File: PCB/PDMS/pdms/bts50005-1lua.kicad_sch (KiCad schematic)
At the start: 11 parts, among them Q3 BTS500101LUAAUMA1

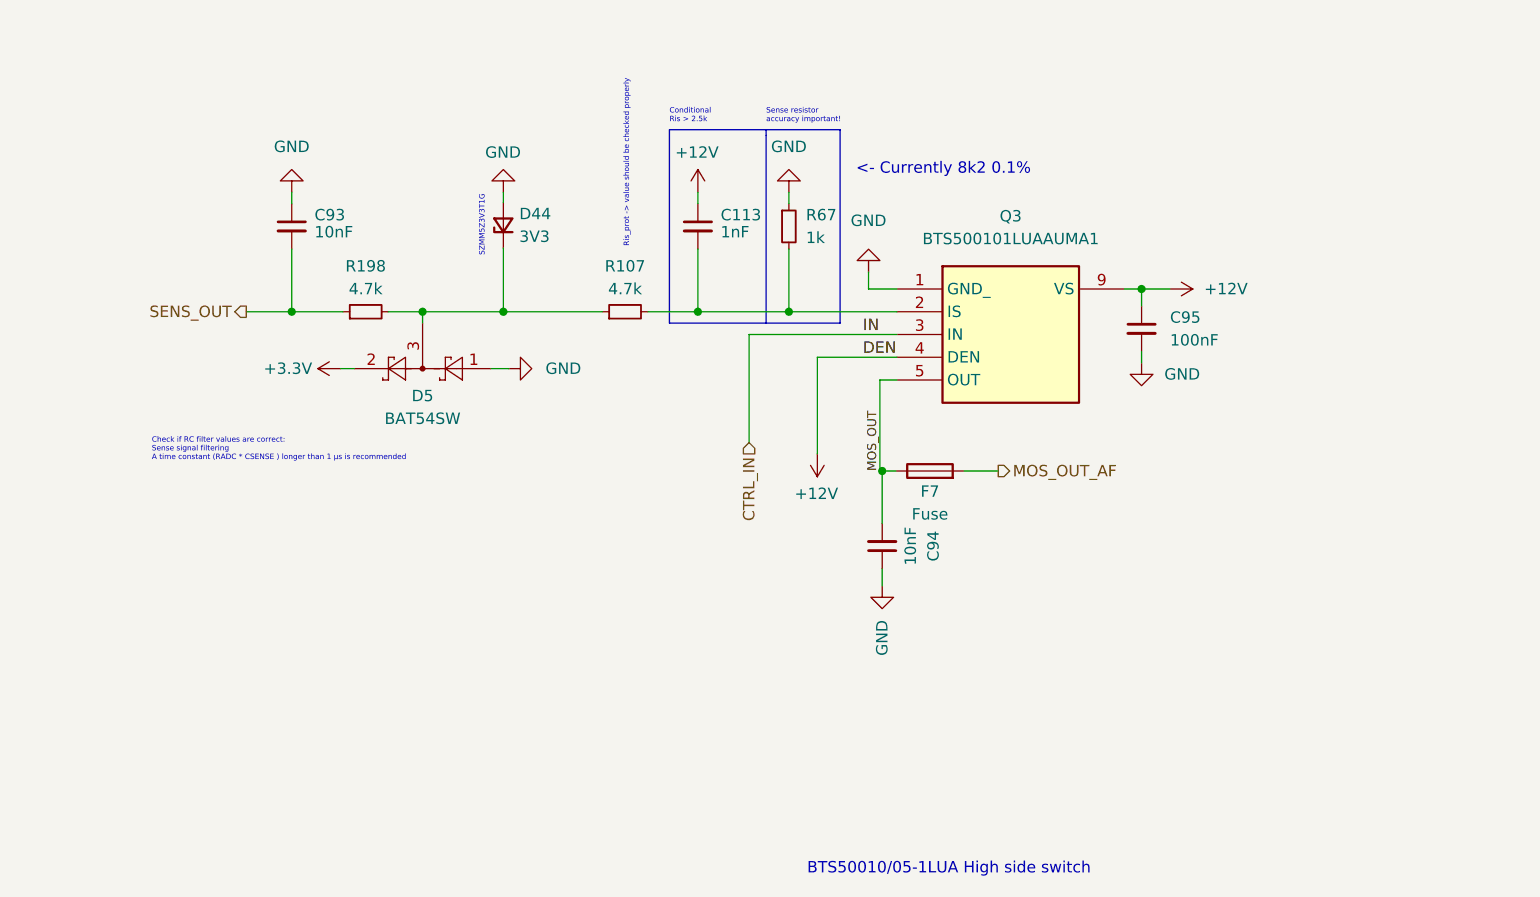
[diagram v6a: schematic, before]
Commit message: WIP PCB folder structure and schematic clean-up
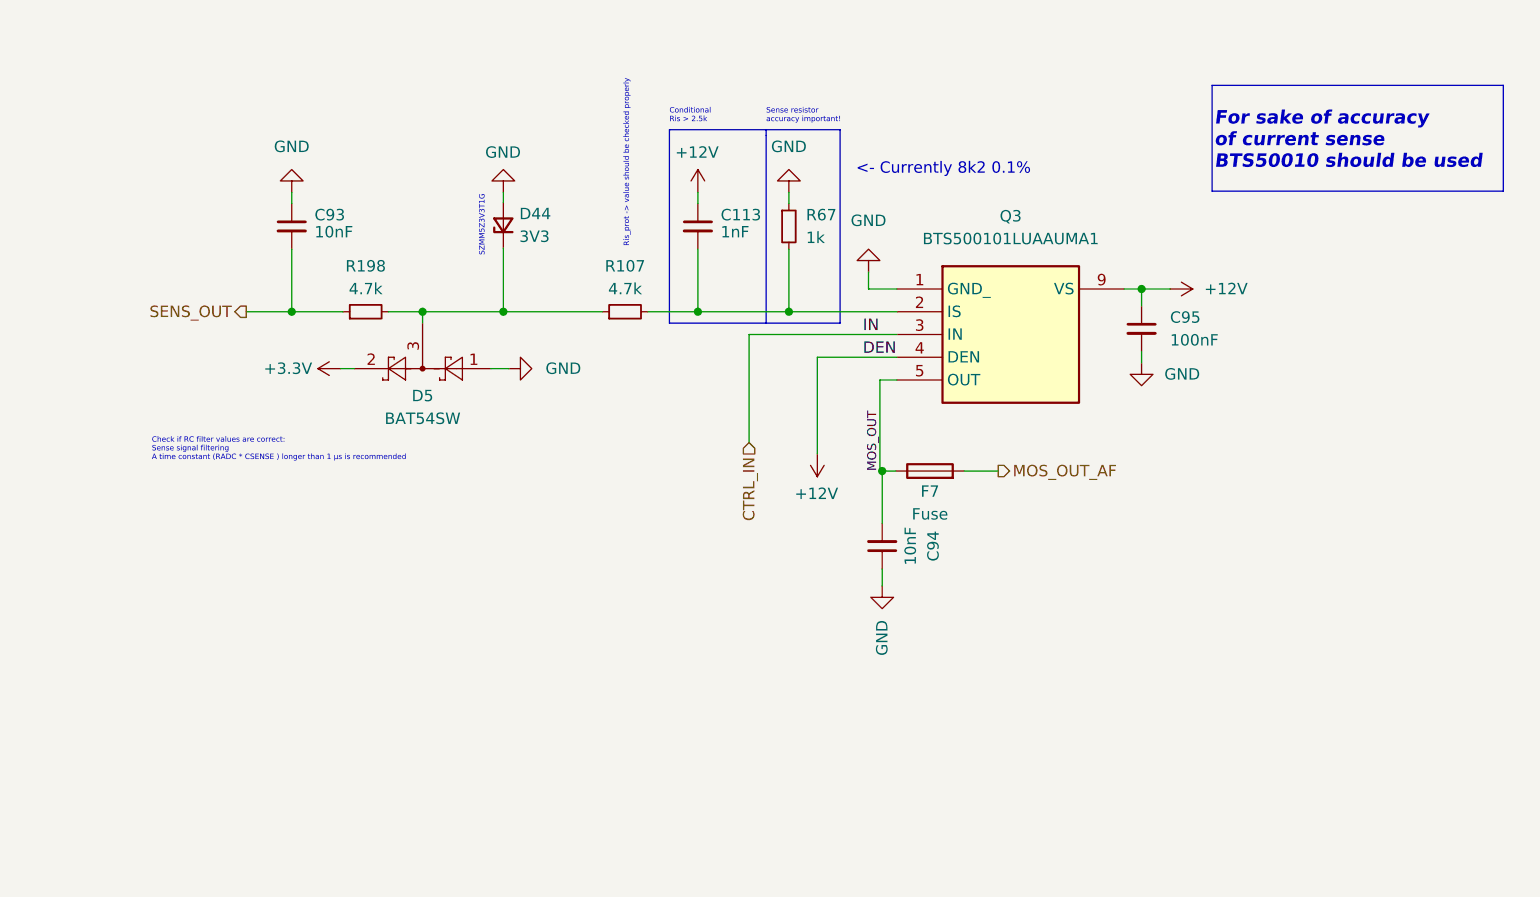
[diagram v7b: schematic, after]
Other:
- note added: "For sake of accuracy of current sense BTS50010 should be used"
- note removed: "BTS50010/05-1LUA High side switch"
- company: (none) -> PGRacing Team
- title: (none) -> BTS50010/05-1LUA High side switch 
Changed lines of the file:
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@@
 (kicad_sch (version 20211123) (generator eeschema)
   (paper "A5")
+  (title_block
+    (title "BTS50010/05-1LUA High side switch ")
+    (rev "V4.2")
+    (company "PGRacing Team")
+    (comment 1 "Karol Pergoł")
+  )
   (junction (at 137.668 62.738) (diameter 0) (color 0 0 0 0)
   )
@@
     (stroke (width 0) (type default) (color 0 0 0 0))
   )
+  (polyline (pts (xy 178.054 40.005) (xy 178.054 51.816))
+    (stroke (width 0) (type default) (color 255 0 0 1))
+  )
   (wire (pts (xy 42.799 51.943) (xy 42.799 53.213))
     (stroke (width 0) (type default) (color 0 0 0 0))
@@
   (wire (pts (xy 108.458 83.058) (xy 108.712 83.058))
     (stroke (width 0) (type default) (color 0 0 0 0))
+  )
+  (polyline (pts (xy 145.542 40.005) (xy 178.054 40.005))
+    (stroke (width 0) (type default) (color 255 0 0 1))
   )
   (wire (pts (xy 108.712 83.058) (xy 110.236 83.058))
@@
   (wire (pts (xy 137.668 70.993) (xy 137.668 69.723))
     (stroke (width 0) (type default) (color 0 0 0 0))
+  )
+  (polyline (pts (xy 145.542 40.005) (xy 145.542 51.816))
+    (stroke (width 0) (type default) (color 255 0 0 1))
   )
   (wire (pts (xy 135.763 62.738) (xy 137.668 62.738))
@@
     (stroke (width 0) (type default) (color 0 0 0 0))
   )
+  (polyline (pts (xy 178.054 51.816) (xy 145.542 51.816))
+    (stroke (width 0) (type default) (color 255 0 0 1))
+  )
   (wire (pts (xy 98.298 51.943) (xy 98.298 53.213))
     (stroke (width 0) (type default) (color 0 0 0 0))
@@
     (effects (font (size 0.6 0.6)) (justify left bottom))
   )
+  (text "For sake of accuracy \nof current sense \nBTS50010 should be used"
+    (at 145.796 49.53 0)
+    (effects (font (size 1.5 1.5) bold italic) (justify left bottom))
+  )
   (text "SZMM5Z3V3T1G " (at 64.389 59.182 90)
     (effects (font (size 0.6 0.6)) (justify left bottom))
@@
     (effects (font (size 0.6 0.6)) (justify left bottom))
   )
-  (text "BTS50010/05-1LUA High side switch " (at 100.33 128.27 0)
-    (effects (font (size 1.27 1.27)) (justify left bottom))
-  )
   (text "Sense resistor\naccuracy important!" (at 95.758 44.323 0)
